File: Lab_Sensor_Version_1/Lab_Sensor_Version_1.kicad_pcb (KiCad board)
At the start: 2 copper layers, 116 x 66 mm, 28 parts, among them U1 ESP32-POE, U2 AM2302, U3 SSD1306, U4 INMP441

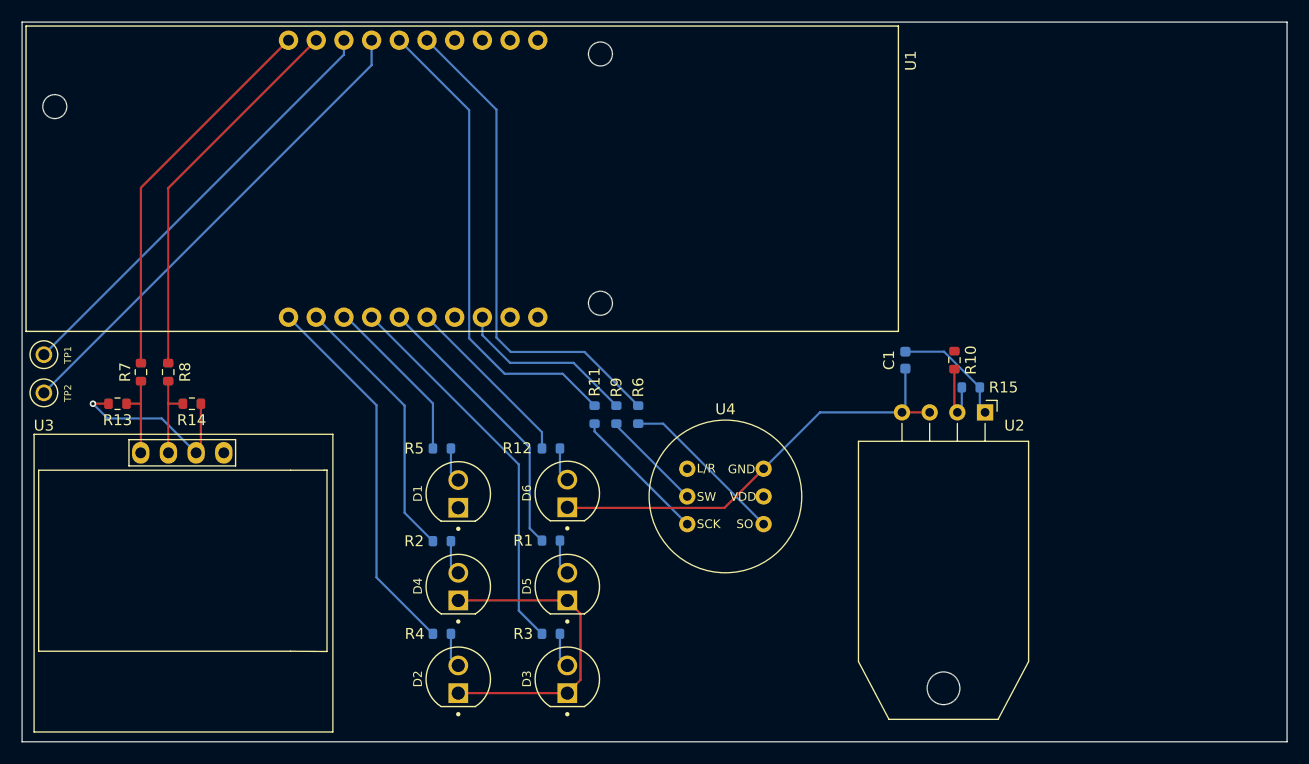
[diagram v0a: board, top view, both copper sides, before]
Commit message: Routed Cables for V1
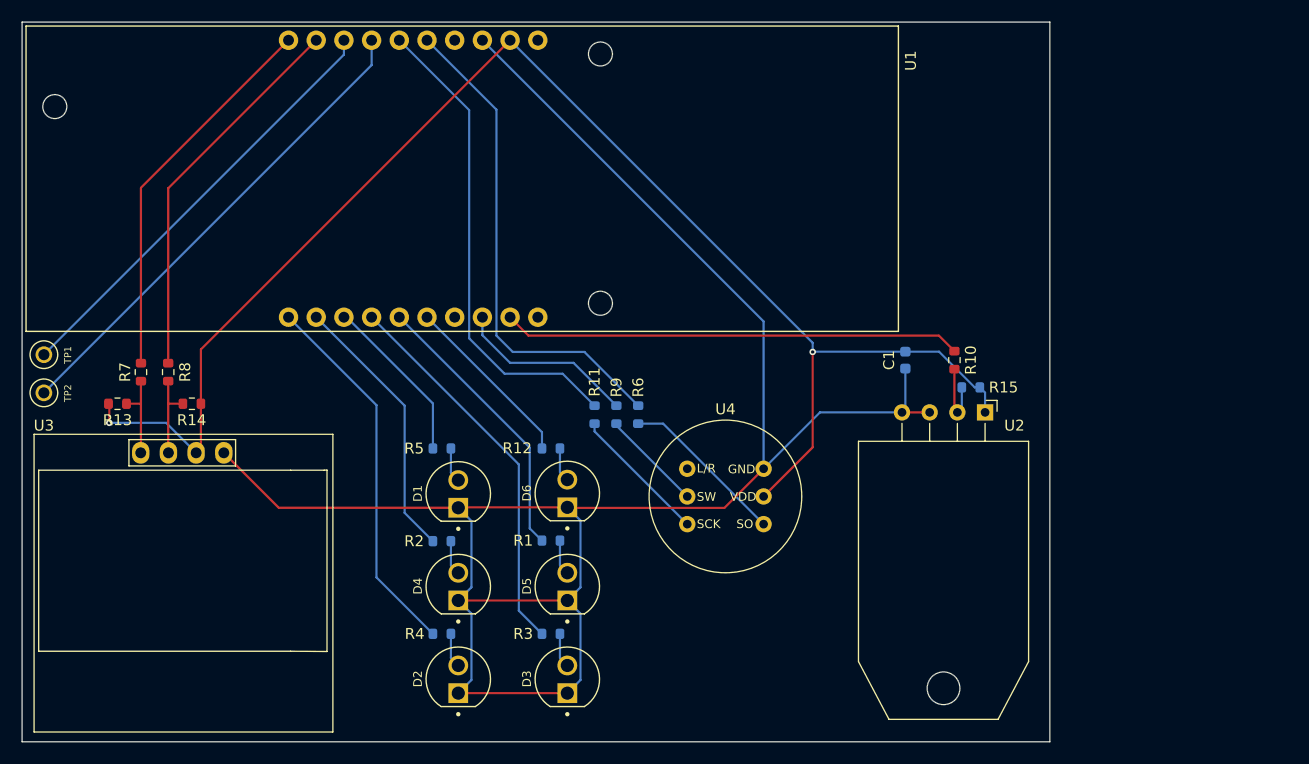
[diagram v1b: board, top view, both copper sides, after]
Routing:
- net GND: track 70.5 -> 182.7 mm
- net +3.3V: track 28.1 -> 135.0 mm, vias 1 -> 2
- net Net-(U1-GPI36): track 0.00 -> 42.0 mm
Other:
- board size 116 x 66 mm -> 94.2 x 66 mm

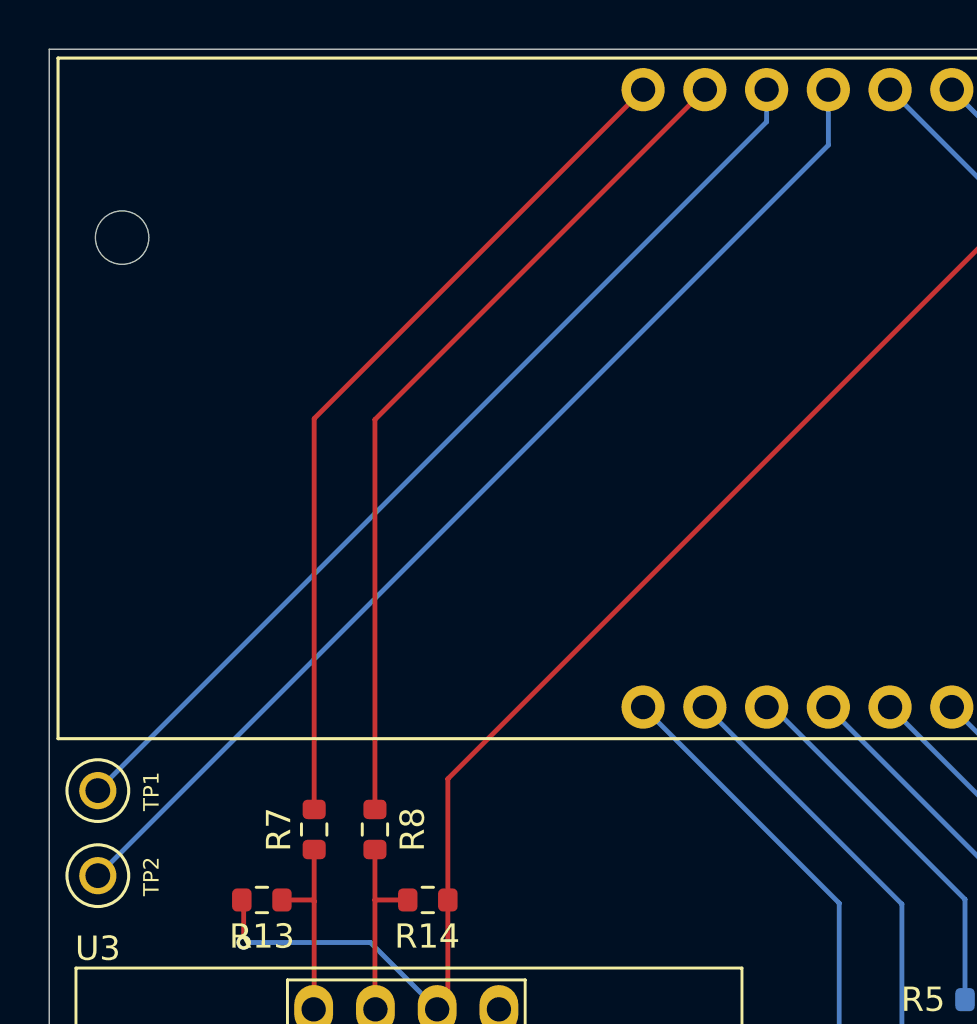
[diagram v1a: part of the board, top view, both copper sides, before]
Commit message: Rerouted 4 GPIO expanders
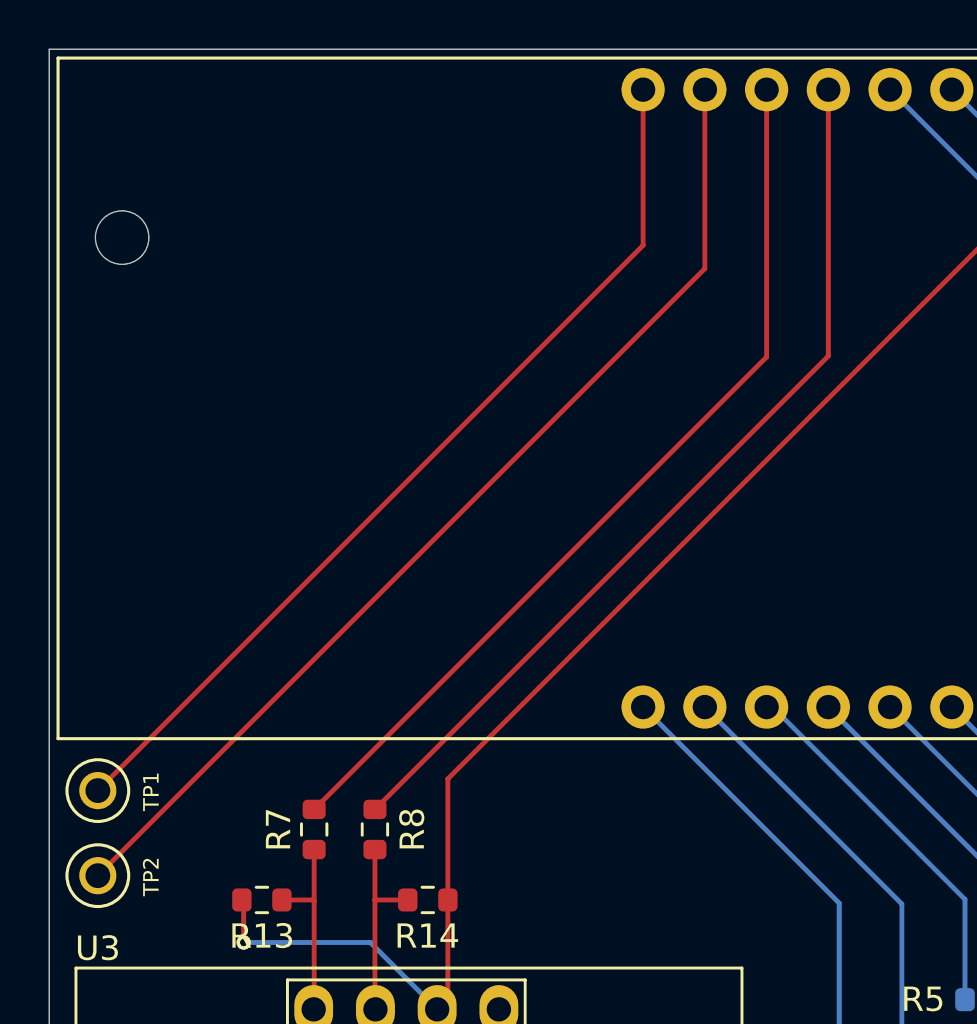
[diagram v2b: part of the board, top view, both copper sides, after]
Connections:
- R7 pad 2: Net-(U1-GPIO5) -> Net-(U1-GPIO3)
- R8 pad 2: Net-(U1-GPIO4) -> Net-(U1-GPIO2)
- TP1 pad TP: Net-(U1-GPIO3) -> Net-(U1-GPIO5)
- TP2 pad TP: Net-(U1-GPIO2) -> Net-(U1-GPIO4)
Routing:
- net Net-(U1-GPIO4): track 35.2 -> 42.7 mm
- net Net-(U1-GPIO2): track 44.8 -> 37.3 mm
- net Net-(U1-GPIO5): track 35.2 -> 38.1 mm
- net Net-(U1-GPIO3): track 40.2 -> 37.3 mm
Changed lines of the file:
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@@
 			(layers "*.Cu" "*.Mask")
 			(remove_unused_layers no)
-			(net 4 "Net-(U1-GPIO2)")
+			(net 6 "Net-(U1-GPIO4)")
 			(pintype "passive")
 			(solder_mask_margin 0.102)
@@
 			(layers "*.Cu" "*.Mask")
 			(remove_unused_layers no)
-			(net 5 "Net-(U1-GPIO3)")
+			(net 7 "Net-(U1-GPIO5)")
 			(pintype "passive")
 			(solder_mask_margin 0.102)
@@
 			(layers "F.Cu" "F.Mask" "F.Paste")
 			(roundrect_rratio 0.25)
-			(net 7 "Net-(U1-GPIO5)")
+			(net 5 "Net-(U1-GPIO3)")
 			(pintype "passive")
 		)
@@
 			(layers "F.Cu" "F.Mask" "F.Paste")
 			(roundrect_rratio 0.25)
-			(net 6 "Net-(U1-GPIO4)")
+			(net 4 "Net-(U1-GPIO2)")
 			(pintype "passive")
 		)
@@
 	)
 	(segment
-		(start 107.053 50.447)
-		(end 77 80.5)
+		(start 107.053 48.164)
+		(end 107.053 59.122)
 		(width 0.2)
-		(layer "B.Cu")
+		(layer "F.Cu")
 		(net 4)
 	)
 	(segment
-		(start 107.053 48.164)
-		(end 107.053 50.447)
+		(start 107.053 59.122)
+		(end 88.4 77.775)
 		(width 0.2)
-		(layer "B.Cu")
+		(layer "F.Cu")
 		(net 4)
 	)
 	(segment
-		(start 104.513 49.487)
-		(end 77 77)
+		(start 104.513 48.164)
+		(end 104.513 59.162)
 		(width 0.2)
-		(layer "B.Cu")
+		(layer "F.Cu")
 		(net 5)
 	)
 	(segment
-		(start 104.513 48.164)
-		(end 104.513 49.487)
+		(start 104.513 59.162)
+		(end 85.9 77.775)
 		(width 0.2)
-		(layer "B.Cu")
+		(layer "F.Cu")
 		(net 5)
 	)
 	(segment
-		(start 88.4 77.775)
-		(end 88.4 61.737)
+		(start 77 80.5)
+		(end 101.973 55.527)
 		(width 0.2)
 		(layer "F.Cu")
@@
 	)
 	(segment
-		(start 88.4 61.737)
+		(start 101.973 55.527)
 		(end 101.973 48.164)
 		(width 0.2)
@@
 	)
 	(segment
-		(start 85.9 77.775)
-		(end 85.9 61.697)
+		(start 99.433 48.164)
+		(end 99.433 54.567)
 		(width 0.2)
 		(layer "F.Cu")
@@
 	)
 	(segment
-		(start 85.9 61.697)
-		(end 99.433 48.164)
+		(start 99.433 54.567)
+		(end 77 77)
 		(width 0.2)
 		(layer "F.Cu")
